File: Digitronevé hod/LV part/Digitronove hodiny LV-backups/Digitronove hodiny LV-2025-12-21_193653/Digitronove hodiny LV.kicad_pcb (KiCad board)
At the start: 2 copper layers, 18.3 x 10.2 mm, 0 parts

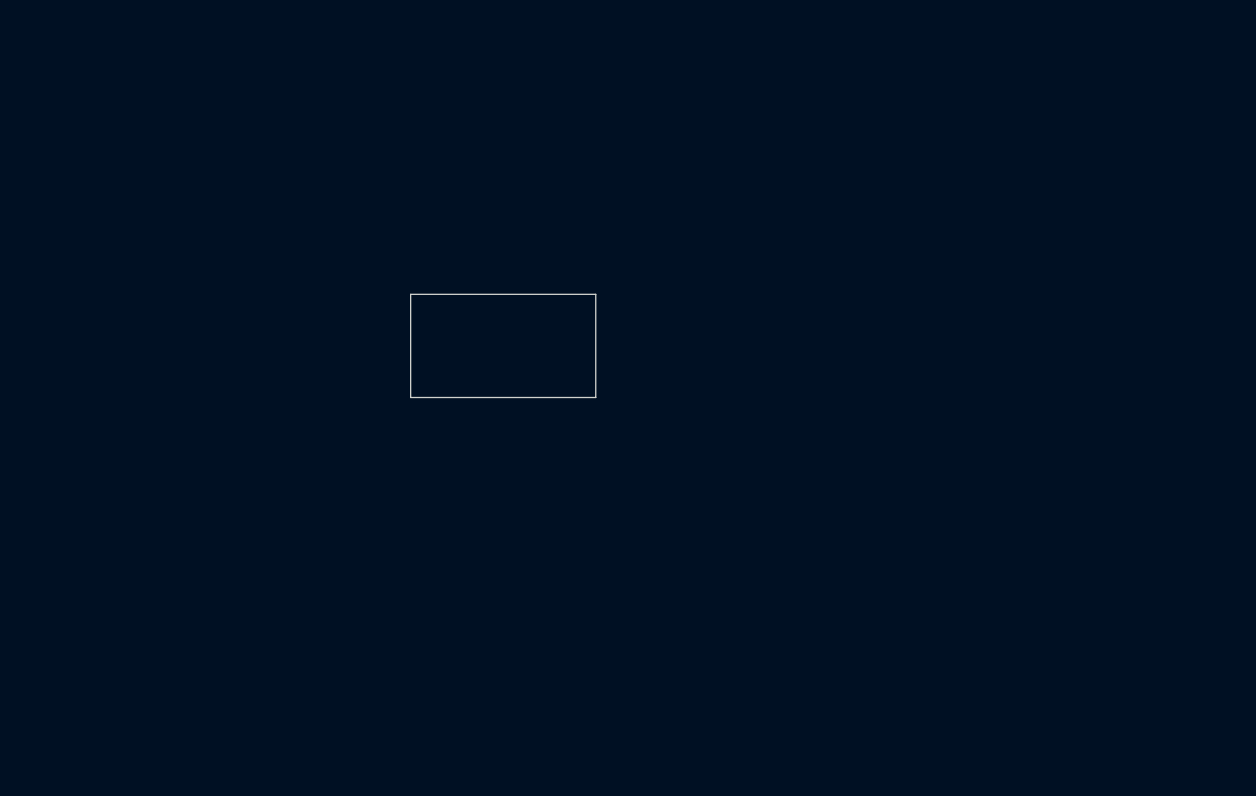
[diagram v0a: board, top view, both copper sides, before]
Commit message: schéma LV desky update
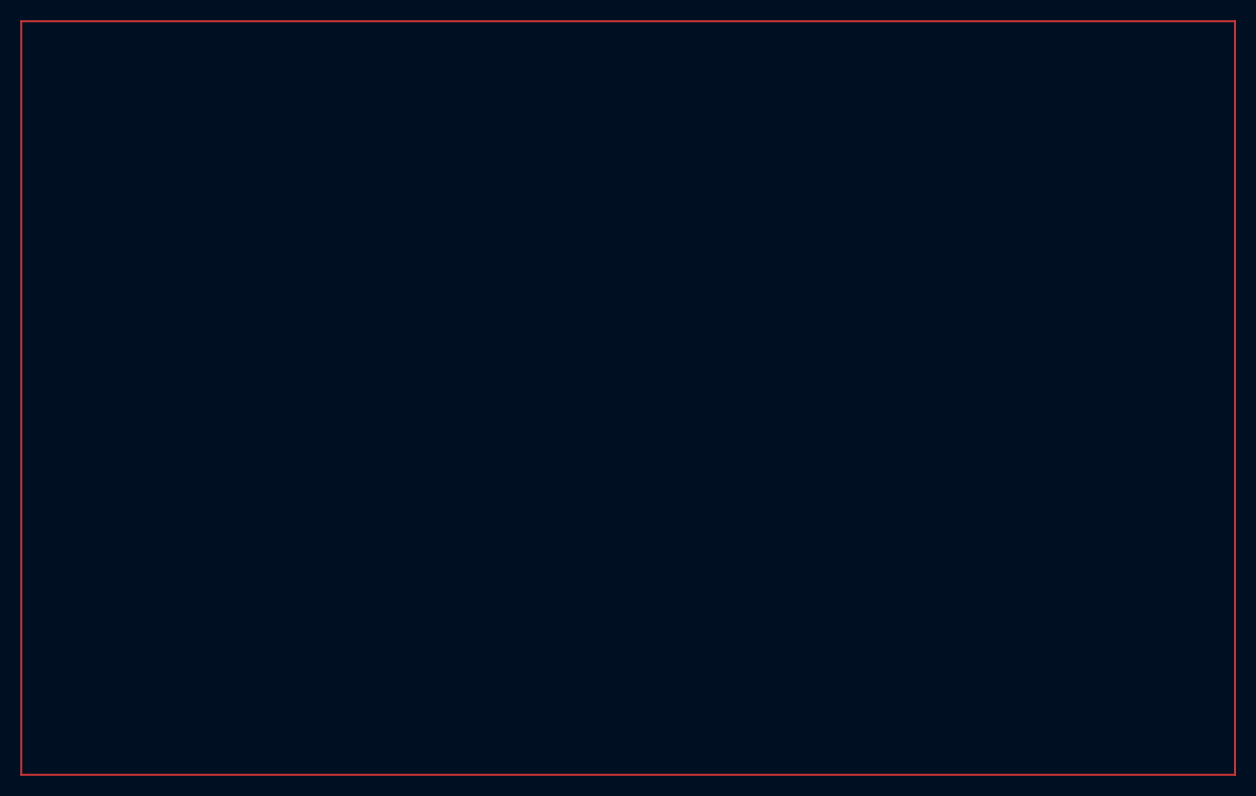
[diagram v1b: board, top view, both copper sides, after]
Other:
- board outline removed
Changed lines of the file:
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@@
 	(net 0 "")
 	(gr_rect
-		(start 135.5 76.5)
-		(end 153.8 86.7)
+		(start 97 49.5)
+		(end 217 124)
 		(stroke
-			(width 0.05)
-			(type solid)
+			(width 0.2)
+			(type default)
 		)
 		(fill no)
-		(layer "Edge.Cuts")
+		(layer "F.Cu")
 	)
 	(embedded_fonts no)
